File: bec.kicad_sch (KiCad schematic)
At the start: 17 parts, among them J3 From BEC, J4 From Battery, U4 TPS5430DDA

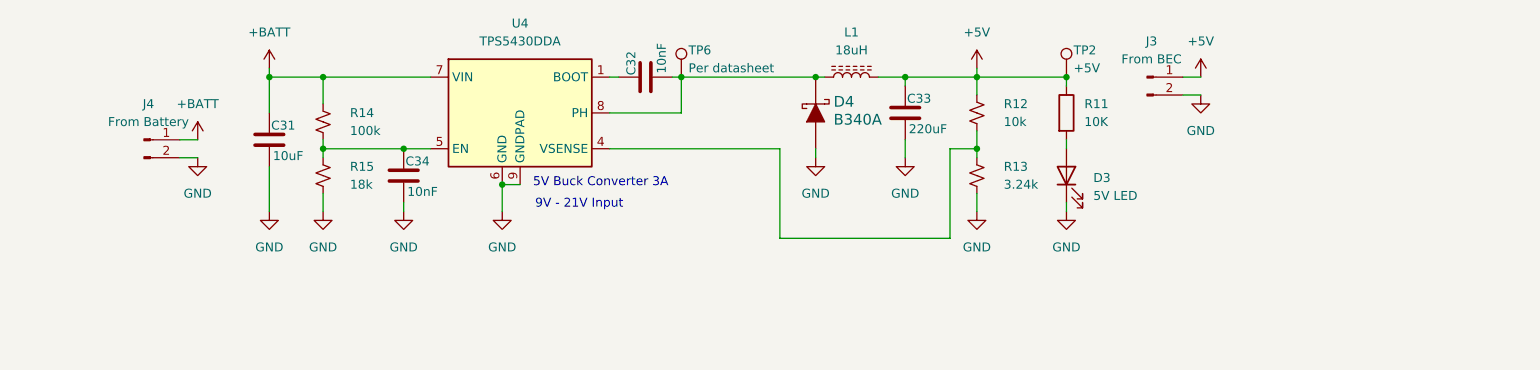
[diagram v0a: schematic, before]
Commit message: move BEC to new sheet
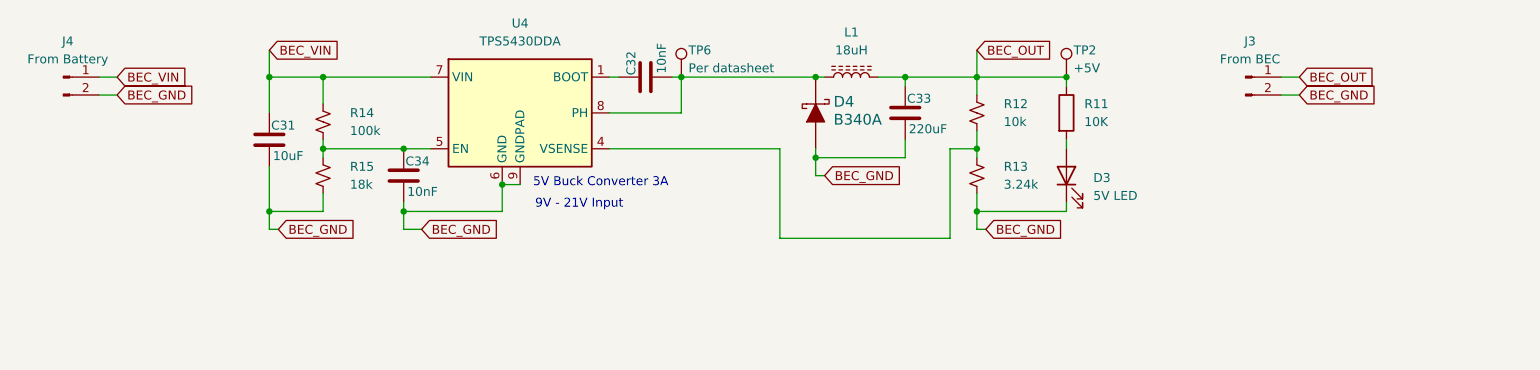
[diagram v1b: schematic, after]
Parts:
- D3: footprint LED_SMD:LED_0402_1005Metric -> LED_SMD:LED_0805_2012Metric_Pad1.15x1.40mm_HandSolder
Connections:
- net +5V renamed BEC_OUT
- net +BATT renamed BEC_VIN
- net GND renamed BEC_GND
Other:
- moved on the sheet: J3, J4

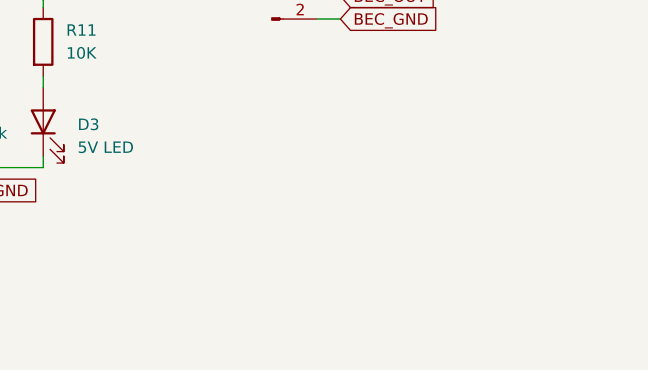
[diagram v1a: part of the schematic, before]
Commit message: df13 connectors and more connectors for the bec
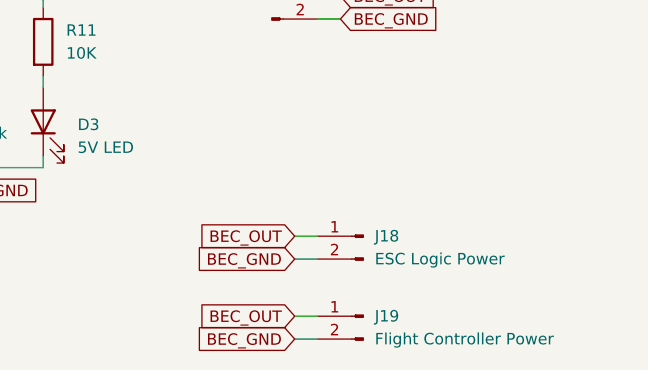
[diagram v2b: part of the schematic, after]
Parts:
- added J18: ESC Logic Power, Connector_Hirose:Hirose_DF13-02P-1.25DS_1x02_P1.25mm_Horizontal, symbol Connector:Conn_01x02_Pin
- added J19: Flight Controller Power, Connector_Hirose:Hirose_DF13-02P-1.25DS_1x02_P1.25mm_Horizontal, symbol Connector:Conn_01x02_Pin
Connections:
- net BEC_GND: now also J18.2 (Pin_2), J19.2 (Pin_2)
- net BEC_OUT: now also J18.1 (Pin_1), J19.1 (Pin_1)
